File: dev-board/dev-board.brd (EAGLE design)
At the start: 49.2 x 64.8 mm, 44 parts, among them J1 12401832E402A, U1 STM32F103RET6, U2 AT24C64BN-10SU-2.7, U3 FT232RL, U4 MCP2551, U5 LM1117IMP-3.3, X1 8MHz

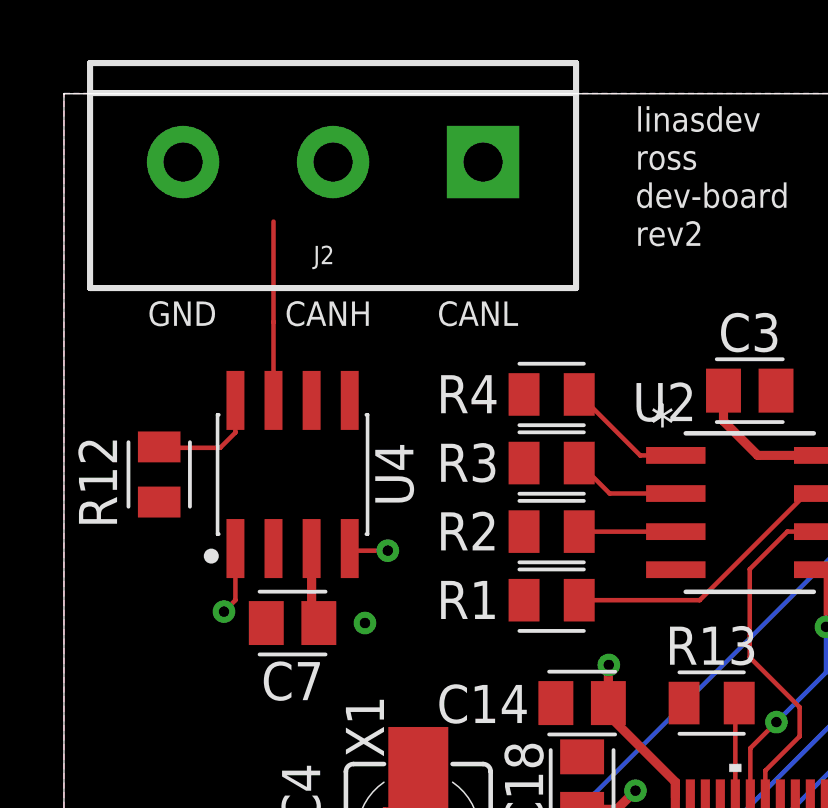
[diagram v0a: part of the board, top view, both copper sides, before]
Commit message: Fix up dev-board mcp2551 pcb area
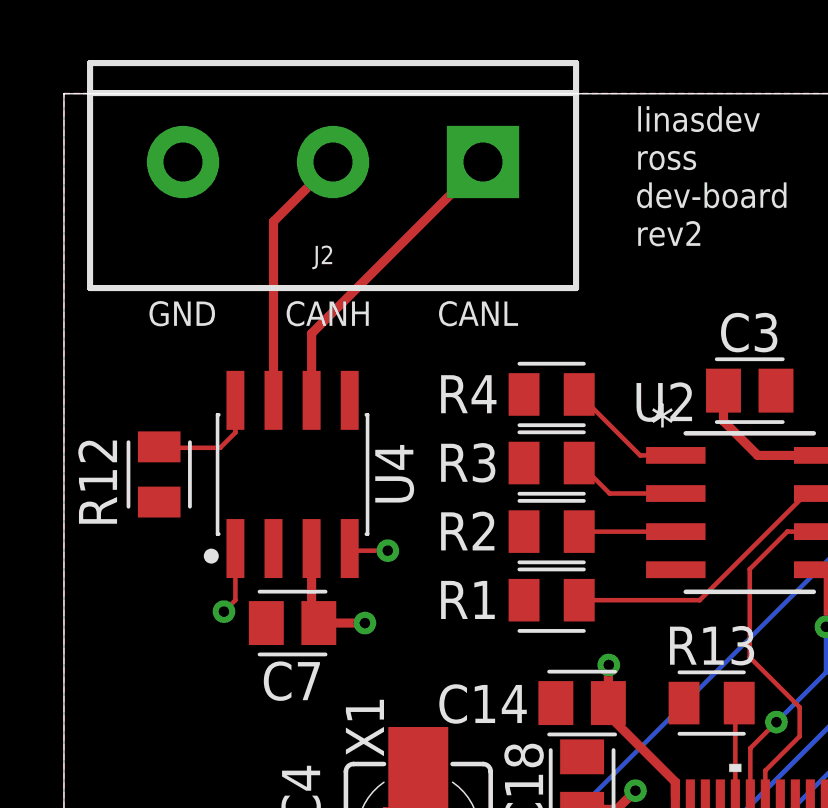
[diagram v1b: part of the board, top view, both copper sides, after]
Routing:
- net CANL: track 0.00 -> 10.3 mm
- net CANH: track 5.96 -> 8.77 mm
- net +5V: track 117.6 -> 119.1 mm
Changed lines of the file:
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@@
 <wire x1="22.2060125" y1="15.113" x2="27.432" y2="15.113" width="0.3048" layer="15"/>
 <wire x1="14.351" y1="5.588" x2="14.351" y2="6.8716" width="0.3048" layer="1"/>
-<wire x1="5.715" y1="47.3574" x2="5.9554" y2="47.117" width="0" layer="19" extent="1-1"/>
-<wire x1="7.493" y1="47.117" x2="5.9554" y2="47.117" width="0" layer="19" extent="1-1"/>
+<wire x1="5.9554" y1="47.117" x2="7.493" y2="47.117" width="0.3048" layer="1"/>
+<wire x1="5.9554" y1="47.117" x2="5.715" y2="47.3574" width="0" layer="19" extent="1-1"/>
 <wire x1="14.1244" y1="6.645" x2="14.351" y2="6.8716" width="0" layer="19" extent="1-1"/>
 <wire x1="24.779" y1="13.004" x2="24.779" y2="13.385" width="0" layer="19" extent="1-1"/>
@@
 <contactref element="J2" pad="2"/>
 <contactref element="U4" pad="7"/>
-<wire x1="4.445" y1="54.5393" x2="4.445" y2="57.15" width="0.1524" layer="1"/>
-<wire x1="4.445" y1="57.15" x2="4.445" y2="60.499" width="0.1524" layer="1"/>
-<wire x1="4.445" y1="57.15" x2="6.43" y2="62.484" width="0" layer="19" extent="1-1"/>
+<wire x1="4.445" y1="54.5393" x2="4.445" y2="60.499" width="0.3048" layer="1"/>
+<wire x1="4.445" y1="60.499" x2="6.43" y2="62.484" width="0.3048" layer="1"/>
 </signal>
 <signal name="CANL">
 <contactref element="J2" pad="1"/>
 <contactref element="U4" pad="6"/>
-<wire x1="5.715" y1="54.5393" x2="11.43" y2="62.484" width="0" layer="19" extent="1-1"/>
+<wire x1="5.715" y1="54.5393" x2="5.715" y2="56.769" width="0.3048" layer="1"/>
+<wire x1="5.715" y1="56.769" x2="11.43" y2="62.484" width="0.3048" layer="1"/>
 </signal>
 </signals>

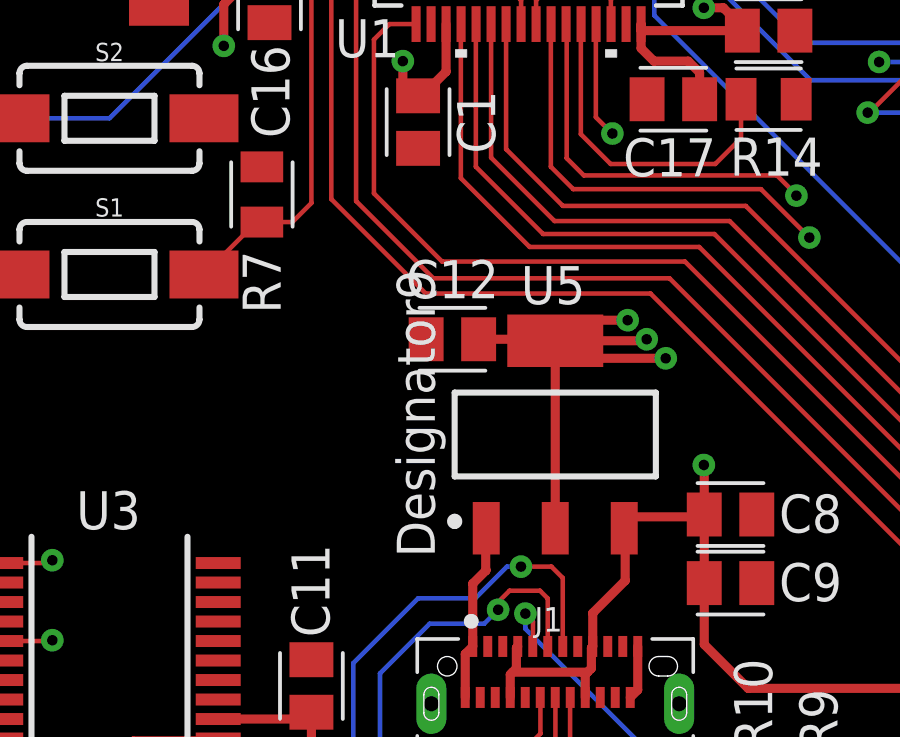
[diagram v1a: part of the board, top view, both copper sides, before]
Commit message: Remove designator labels around regulator in dev-boarc pcb
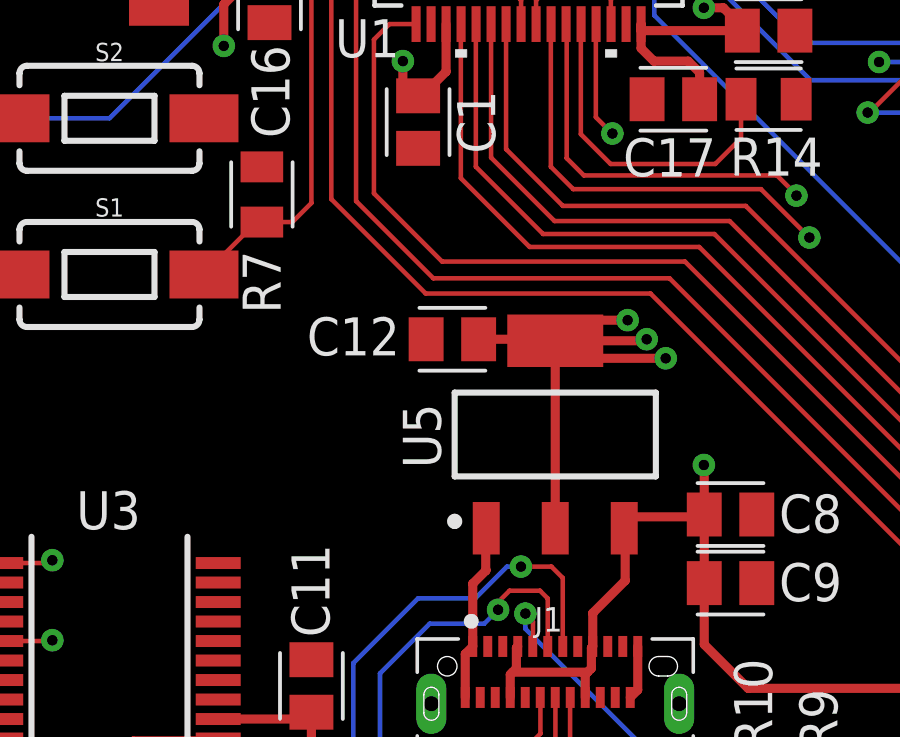
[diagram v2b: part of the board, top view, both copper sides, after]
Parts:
- U5: value LM1117IMP-3.3 -> Value
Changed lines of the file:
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@@
 <attribute name="MANUFACTURER" value="" x="-16.51" y="57.404" size="1.778" layer="27" rot="R180" display="off"/>
 <attribute name="MPN" value="" x="-16.51" y="57.404" size="1.778" layer="27" rot="R180" display="off"/>
-<attribute name="NAME" x="19.05" y="20.6703" size="1.27" layer="25" align="bottom-center"/>
+<attribute name="NAME" x="15.748" y="18.7653" size="1.27" layer="25" align="bottom-center"/>
 <attribute name="OPERATING_TEMP" value="" x="-16.51" y="57.404" size="1.778" layer="27" rot="R180" display="off"/>
 <attribute name="PART_STATUS" value="" x="-16.51" y="57.404" size="1.778" layer="27" rot="R180" display="off"/>
@@
 <attribute name="TYPE" value="" x="25.4" y="69.85" size="1.778" layer="27" rot="R90" display="off"/>
 </element>
-<element name="U5" library="LM1117IMP-3.3" package="DCY0004A_N" value="LM1117IMP-3.3" x="22.479" y="16.129" smashed="yes" rot="R90">
+<element name="U5" library="LM1117IMP-3.3" package="DCY0004A_N" value="Value" x="22.479" y="16.129" smashed="yes" rot="R90">
 <attribute name="MANUFACTURER" value="Texas Instruments" x="30.099" y="72.009" size="1.778" layer="27" rot="R90" display="off"/>
-<attribute name="NAME" x="21.336" y="20.4724" size="1.27" layer="25" ratio="6" rot="SR0"/>
+<attribute name="NAME" x="18.669" y="15.0114" size="1.27" layer="25" ratio="6" rot="SR90"/>
 <attribute name="PARTNUMBER" value="LM1117IMP-3.3/NOPB" x="30.099" y="72.009" size="1.778" layer="27" rot="R90" display="off"/>
 <attribute name="REFDES" value="RefDes" x="30.099" y="72.009" size="1.778" layer="27" rot="R90" display="off"/>

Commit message: Move things around
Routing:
- net +3V3: track 63.1 -> 67.3 mm, vias 11 -> 12
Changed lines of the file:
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@@
 <attribute name="MANUFACTURER" value="" x="66.04" y="-1.27" size="1.778" layer="27" display="off"/>
 <attribute name="MPN" value="" x="66.04" y="-1.27" size="1.778" layer="27" display="off"/>
-<attribute name="NAME" x="19.05" y="45.7281" size="1.27" layer="25" align="bottom-center"/>
+<attribute name="NAME" x="22.225" y="43.8231" size="1.27" layer="25" align="bottom-center"/>
 <attribute name="OPERATING_TEMP" value="" x="66.04" y="-1.27" size="1.778" layer="27" display="off"/>
 <attribute name="PART_STATUS" value="" x="66.04" y="-1.27" size="1.778" layer="27" display="off"/>
@@
 <attribute name="BUILT_BY" value="EMA_UL_Team" x="50.8" y="6.35" size="1.778" layer="27" display="off"/>
 <attribute name="MANUFACTURER_PART_NUMBER" value="AT24C64BN-10SU-2.7" x="50.8" y="6.35" size="1.778" layer="27" display="off"/>
-<attribute name="NAME" x="16.4084" y="53.848" size="1.27" layer="25" ratio="6" rot="SR0"/>
+<attribute name="NAME" x="19.2024" y="46.609" size="1.27" layer="25" ratio="6" rot="SR0"/>
 <attribute name="SOURCELIBRARY" value="Atmel_2015-02-13" x="50.8" y="6.35" size="1.778" layer="27" display="off"/>
 <attribute name="VENDOR" value="Atmel" x="50.8" y="6.35" size="1.778" layer="27" display="off"/>
@@
 <via x="26.162" y="18.669" extent="1-16" drill="0.35"/>
 <wire x1="25.477" y1="19.254" x2="23.191" y2="19.254" width="0.3048" layer="1"/>
+<wire x1="10.77" y1="26.67" x2="12.3905" y2="25.0495" width="0.1524" layer="1"/>
+<wire x1="12.7" y1="25.0495" x2="11.5875" y2="25.0495" width="0.1524" layer="1"/>
+<wire x1="11.5875" y1="25.0495" x2="11.049" y2="24.511" width="0.1524" layer="1"/>
+<via x="11.049" y="24.511" extent="1-16" drill="0.35"/>
 <wire x1="27.0815" y1="49.657" x2="27.0815" y2="51.943" width="0" layer="19" extent="1-1"/>
 <wire x1="22.785" y1="52.705" x2="27.0815" y2="51.943" width="0" layer="19" extent="1-1"/>
@@
 <wire x1="15.84" y1="33.31" x2="15.84" y2="39.31" width="0" layer="19" extent="1-1"/>
 <wire x1="10.77" y1="26.67" x2="11.43" y2="29.083" width="0" layer="19" extent="1-1"/>
-<wire x1="12.3905" y1="25.0495" x2="10.77" y2="26.67" width="0" layer="19" extent="1-1"/>
 <wire x1="18.84" y1="29.81" x2="15.84" y2="33.31" width="0" layer="19" extent="1-1"/>
 <wire x1="25.34" y1="29.81" x2="18.84" y2="29.81" width="0" layer="19" extent="1-1"/>
 <wire x1="24.892" y1="19.939" x2="27.2914" y2="27.305" width="0" layer="19" extent="1-1"/>
 <wire x1="27.34" y1="39.31" x2="27.432" y2="30.353" width="0" layer="19" extent="1-1"/>
-<wire x1="3.995" y1="9.895" x2="12.3905" y2="25.0495" width="0" layer="19" extent="1-1"/>
+<wire x1="3.995" y1="9.895" x2="11.049" y2="24.511" width="0" layer="19" extent="1-1"/>
 </signal>
 <signal name="N$1">
@@
 <contactref element="R5" pad="1"/>
 <contactref element="U1" pad="58"/>
-<wire x1="22.785" y1="50.165" x2="23.4645" y2="50.165" width="0.1524" layer="1"/>
-<wire x1="23.4645" y1="50.165" x2="25.2425" y2="51.943" width="0.1524" layer="1"/>
+<wire x1="22.785" y1="50.165" x2="23.8455" y2="50.165" width="0.1524" layer="1"/>
+<wire x1="25.2425" y1="51.562" x2="23.8455" y2="50.165" width="0.1524" layer="1"/>
+<wire x1="25.2425" y1="51.562" x2="25.2425" y2="51.943" width="0.1524" layer="1"/>
 <wire x1="20.84" y1="41.31" x2="20.84" y2="42.199" width="0.1524" layer="1"/>
 <wire x1="20.84" y1="42.199" x2="21.983" y2="43.342" width="0.1524" layer="1"/>
@@
 <wire x1="22.86" y1="48.895" x2="24.4805" y2="48.895" width="0.1524" layer="1"/>
 <wire x1="24.4805" y1="48.895" x2="25.2425" y2="49.657" width="0.1524" layer="1"/>
-<wire x1="20.34" y1="41.31" x2="20.34" y2="42.946" width="0.1524" layer="1"/>
-<wire x1="20.34" y1="42.946" x2="21.209" y2="43.815" width="0.1524" layer="1"/>
-<via x="21.209" y="43.815" extent="1-16" drill="0.35"/>
-<wire x1="21.209" y1="43.815" x2="22.86" y2="45.466" width="0.1524" layer="16"/>
-<wire x1="22.86" y1="45.466" x2="22.86" y2="46.99" width="0.1524" layer="16"/>
+<wire x1="20.34" y1="41.31" x2="20.34" y2="42.692" width="0.1524" layer="1"/>
+<wire x1="20.34" y1="42.692" x2="20.828" y2="43.18" width="0.1524" layer="1"/>
+<via x="20.828" y="43.18" extent="1-16" drill="0.35"/>
+<wire x1="20.828" y1="43.18" x2="22.86" y2="45.212" width="0.1524" layer="16"/>
+<wire x1="22.86" y1="45.212" x2="22.86" y2="46.99" width="0.1524" layer="16"/>
 <via x="22.86" y="46.99" extent="1-16" drill="0.35"/>
 <wire x1="22.86" y1="46.99" x2="22.86" y2="48.895" width="0.1524" layer="1"/>
@@
 <contactref element="U1" pad="14"/>
 <contactref element="JP2" pad="1"/>
-<wire x1="41.91" y1="10.16" x2="40.770925" y2="10.16" width="0.1524" layer="1"/>
-<wire x1="40.770925" y1="10.16" x2="39.780325" y2="9.1694" width="0.1524" layer="1"/>
-<wire x1="39.780325" y1="9.1694" x2="37.3126" y2="9.1694" width="0.1524" layer="1"/>
-<wire x1="37.3126" y1="9.1694" x2="25.654" y2="20.828" width="0.1524" layer="1"/>
+<wire x1="41.91" y1="10.16" x2="41.91" y2="10.156075" width="0.1524" layer="1"/>
+<wire x1="41.91" y1="10.156075" x2="40.669325" y2="8.9154" width="0.1524" layer="1"/>
+<wire x1="40.669325" y1="8.9154" x2="37.5666" y2="8.9154" width="0.1524" layer="1"/>
+<wire x1="37.5666" y1="8.9154" x2="25.654" y2="20.828" width="0.1524" layer="1"/>
 <wire x1="25.654" y1="20.828" x2="18.161" y2="20.828" width="0.1524" layer="1"/>
 <wire x1="15.0145" y1="32.5570875" x2="15.2754125" y2="32.818" width="0.1524" layer="1"/>
